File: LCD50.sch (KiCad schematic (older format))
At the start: 36 parts, among them Q10 IRLML2502, Q8 IRLML2502, Q9 IRLML2502, U20 xc7z020clg484

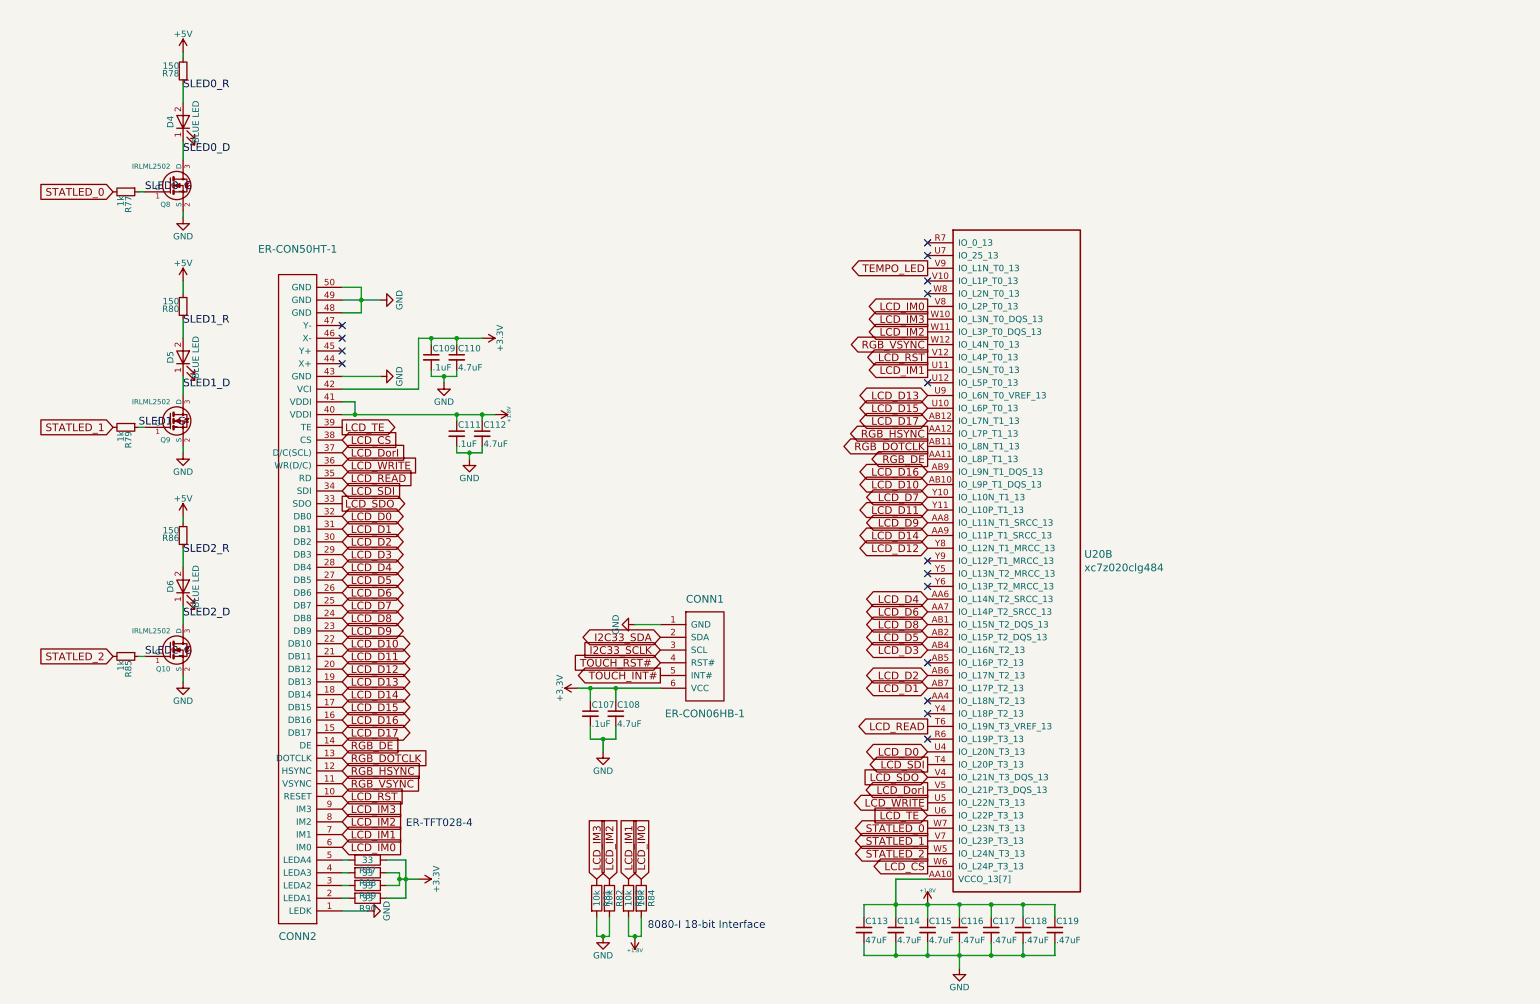
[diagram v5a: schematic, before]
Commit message: everything placed, about to shrink text size globally
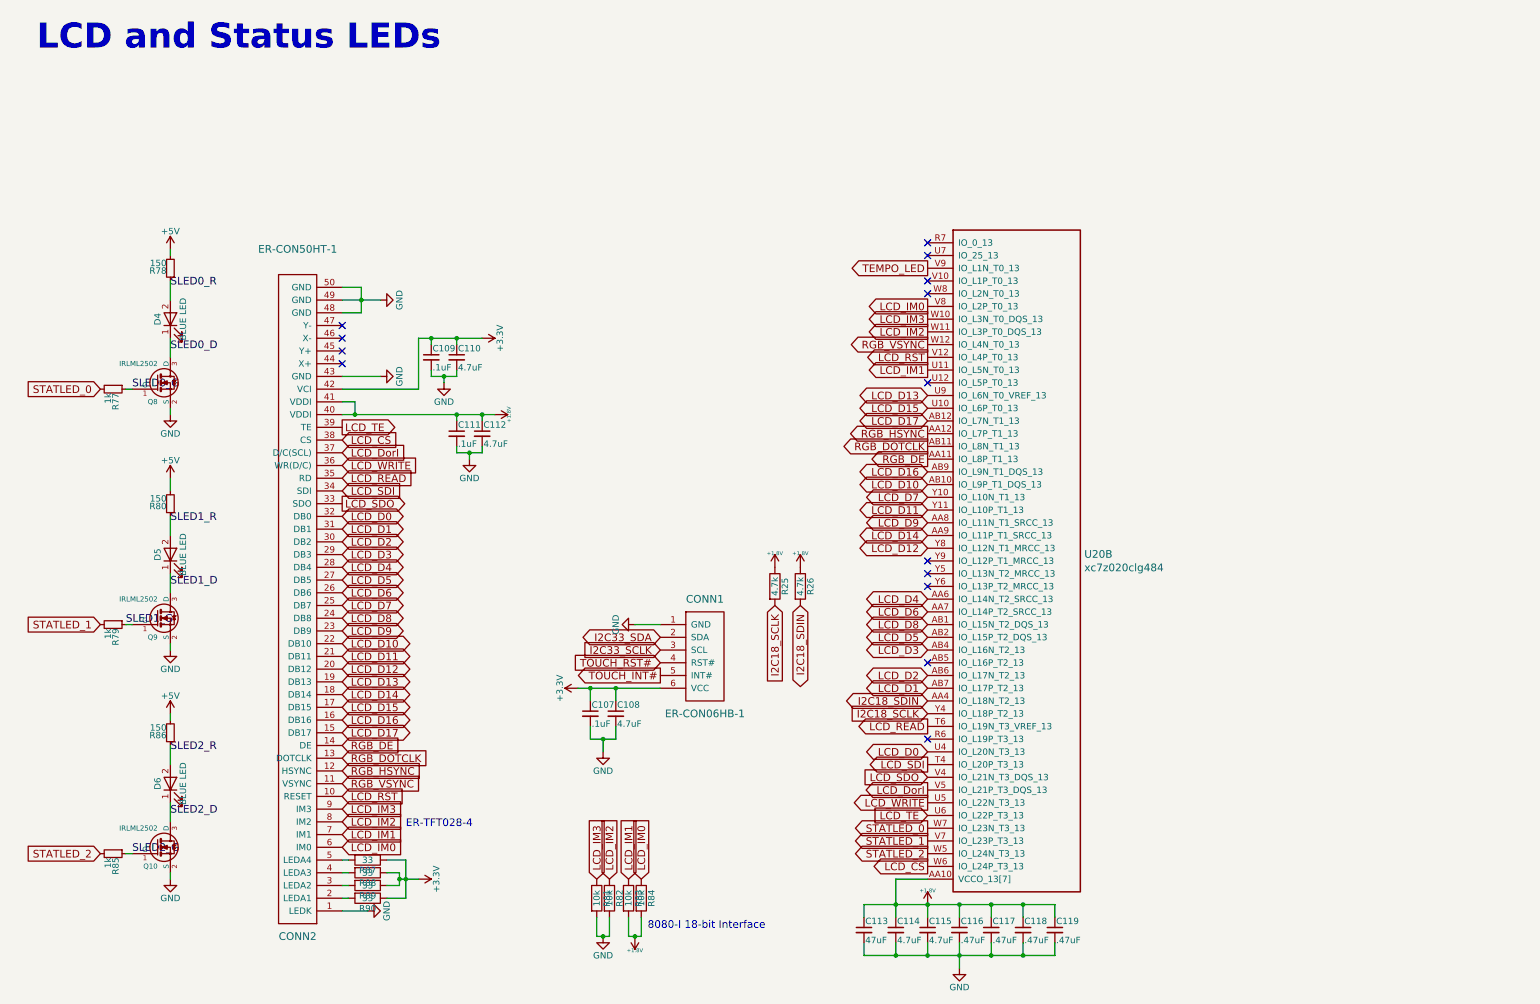
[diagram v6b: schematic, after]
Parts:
- added R25, R26: 4.7k, Resistor_SMD:R_0402_1005Metric, symbol Device:R
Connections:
- net +1V8: now also R25.1, R26.1
- net I2C18_SDIN: now reaches U20.AA4 (IO_L18N_T2_13)
- net I2C18_SDIN: now also R26.2
- net I2C18_SCLK: now reaches U20.Y4 (IO_L18P_T2_13)
- net I2C18_SCLK: now also R25.2
- no-connect marks 16 -> 14
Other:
- note added: "LCD and Status LEDs"
- moved on the sheet: D4, D5, D6, Q10, Q8, Q9, R77, R78, R79, R80, R85, R86
